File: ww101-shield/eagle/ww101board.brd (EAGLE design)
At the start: 65.8 x 74.3 mm, 66 parts, among them J6 U8G-096-OLED, J7 0, U7 CY8C4A45-48

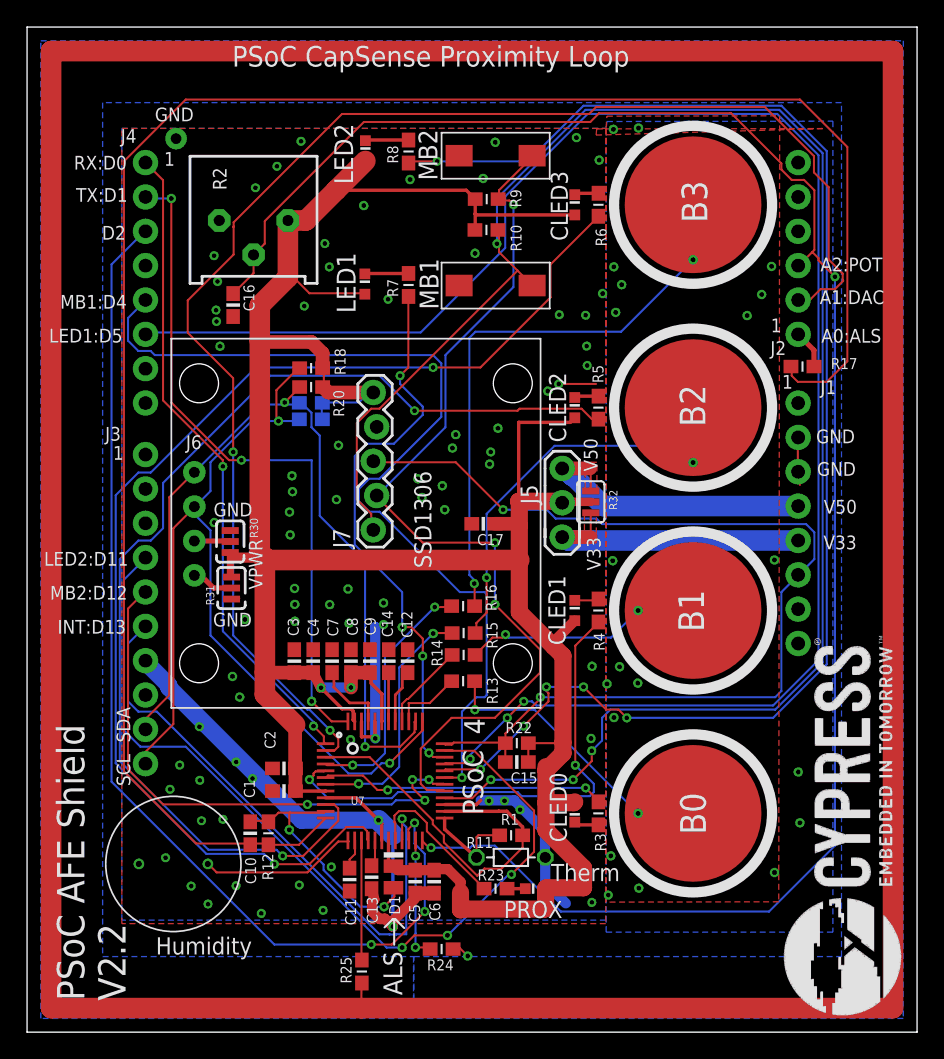
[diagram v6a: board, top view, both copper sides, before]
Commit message: Added R26/R27 Pulldowns on LED pins from arduino
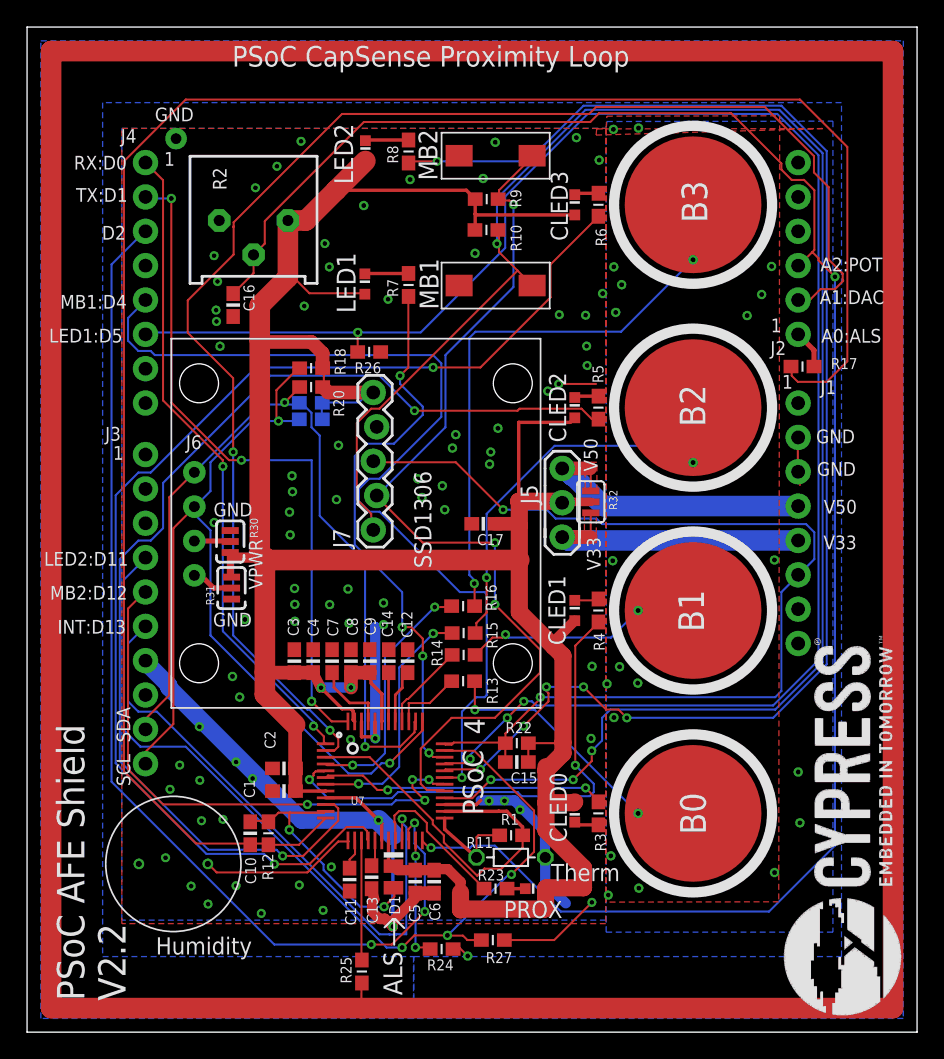
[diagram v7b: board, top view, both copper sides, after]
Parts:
- added R26, R27: 50K, ww101board:0603-RES
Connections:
- net D11: now also R27.2
- net D5: now also R26.2
- net GND: now also R26.1, R27.1
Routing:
- net GND: track 78.2 -> 85.8 mm
- net D11: track 64.8 -> 67.5 mm
- net D5: track 128.6 -> 130.1 mm, vias 3 -> 4
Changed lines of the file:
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@@
 <layer number="14" name="Route14" color="1" fill="6" visible="no" active="no"/>
 <layer number="15" name="Route15" color="4" fill="6" visible="no" active="no"/>
-<layer number="16" name="Bottom" color="1" fill="1" visible="no" active="yes"/>
+<layer number="16" name="Bottom" color="1" fill="1" visible="yes" active="yes"/>
 <layer number="17" name="Pads" color="2" fill="1" visible="yes" active="yes"/>
 <layer number="18" name="Vias" color="2" fill="1" visible="yes" active="yes"/>
@@
 <layer number="21" name="tPlace" color="7" fill="1" visible="yes" active="yes"/>
 <layer number="22" name="bPlace" color="7" fill="1" visible="no" active="yes"/>
-<layer number="23" name="tOrigins" color="15" fill="1" visible="no" active="yes"/>
+<layer number="23" name="tOrigins" color="15" fill="1" visible="yes" active="yes"/>
 <layer number="24" name="bOrigins" color="15" fill="1" visible="no" active="yes"/>
 <layer number="25" name="tNames" color="7" fill="1" visible="yes" active="yes"/>
@@
 </element>
 <element name="U$7" library="ww101board" package="CYLOGO-SILK" value="CYLOGO-SILK" x="58.399678125" y="-8.453115625" rot="R90"/>
+<element name="R26" library="ww101board" package="0603-RES" value="50K" x="19.05" y="40.6146" rot="R180"/>
+<element name="R27" library="ww101board" package="0603-RES" value="50K" x="28.194" y="-2.8702" smashed="yes" rot="R180">
+<attribute name="NAME" x="29.6418" y="-3.7592" size="0.8128" layer="25" font="vector" ratio="15" rot="R180"/>
+<attribute name="VALUE" x="29.718" y="-1.2192" size="0.6096" layer="27" font="vector" ratio="15" rot="R180"/>
+</element>
 </elements>
 <signals>
@@
 <via x="27.9120625" y="7.416803125" extent="1-16" drill="0.3302"/>
 <via x="35.514278125" y="-0.08381875" extent="1-16" drill="0.3302"/>
+<contactref element="R27" pad="1"/>
+<contactref element="R26" pad="1"/>
+<wire x1="29.044" y1="-2.8702" x2="32.727896875" y2="-2.8702" width="0.1524" layer="1"/>
+<wire x1="32.727896875" y1="-2.8702" x2="35.514278125" y2="-0.08381875" width="0.1524" layer="1"/>
 </signal>
 <signal name="XRES">
@@
 <wire x1="29.1084" y1="48.3108" x2="29.1084" y2="52.1208" width="0.1524" layer="16"/>
 <wire x1="22.86" y1="42.0624" x2="29.1084" y2="48.3108" width="0.1524" layer="16"/>
-<wire x1="2.5908" y1="42.0624" x2="22.86" y2="42.0624" width="0.1524" layer="16"/>
+<wire x1="2.5908" y1="42.0624" x2="18.2118" y2="42.0624" width="0.1524" layer="16"/>
+<wire x1="18.2118" y1="42.0624" x2="22.86" y2="42.0624" width="0.1524" layer="16"/>
 <wire x1="24.6888" y1="10.2108" x2="24.63" y2="10.15" width="0.1524" layer="1"/>
 <wire x1="2.5908" y1="42.0624" x2="2.51" y2="41.92" width="0.1524" layer="16"/>
@@
 <via x="29.2608" y="13.5636" extent="1-16" drill="0.3302"/>
 <via x="30.48" y="14.7828" extent="1-16" drill="0.3302"/>
+<contactref element="R26" pad="2"/>
+<wire x1="18.2" y1="40.6146" x2="18.2" y2="42.0506" width="0.1524" layer="1"/>
+<wire x1="18.2" y1="42.0506" x2="18.2118" y2="42.0624" width="0.1524" layer="1"/>
+<via x="18.2118" y="42.0624" extent="1-16" drill="0.35"/>
 </signal>
 <signal name="N$2">
@@
 <wire x1="21.485859375" y1="-3.42391875" x2="20.34031875" y2="-3.42391875" width="0.1524" layer="16"/>
 <wire x1="20.34031875" y1="-3.42391875" x2="5.4864" y2="11.43" width="0.1524" layer="16"/>
+<contactref element="R27" pad="2"/>
+<wire x1="27.344" y1="-2.8702" x2="26.3144" y2="-2.8702" width="0.1524" layer="1"/>
+<wire x1="26.3144" y1="-2.8702" x2="25.9842" y2="-2.54" width="0.1524" layer="1"/>
+<wire x1="25.9842" y1="-2.54" x2="24.8539" y2="-2.54" width="0.1524" layer="1"/>
+<wire x1="24.8539" y1="-2.54" x2="24.83611875" y2="-2.52221875" width="0.1524" layer="1"/>
 </signal>
 <signal name="D12">
